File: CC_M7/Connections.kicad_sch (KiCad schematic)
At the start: 11 parts, among them J1 Conn_01x04_Pin, J10 Conn_01x04_Pin, J11 USB_B_Micro, J12 Conn_01x04_Pin, J3 Conn_01x03_Pin, J4 Conn_01x03_Pin, J5 Conn_01x03_Pin, J6 Conn_01x03_Pin, J7 Conn_01x03_Pin, J8 Conn_01x03_Pin

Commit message: 1x04 connectors chosen and added
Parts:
- J1, J10, J12: footprint Connector_PinHeader_1.27mm:PinHeader_1x04_P1.27mm_Vertical -> Connector_Hirose:Hirose_DF13-04P-1.25DSA_1x04_P1.25mm_Vertical
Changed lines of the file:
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@@
 			)
 		)
-		(property "Footprint" "Connector_PinHeader_1.27mm:PinHeader_1x04_P1.27mm_Vertical"
+		(property "Footprint" "Connector_Hirose:Hirose_DF13-04P-1.25DSA_1x04_P1.25mm_Vertical"
 			(at 142.24 157.48 0)
 			(effects
@@
 			)
 		)
-		(property "Footprint" "Connector_PinHeader_1.27mm:PinHeader_1x04_P1.27mm_Vertical"
+		(property "Footprint" "Connector_Hirose:Hirose_DF13-04P-1.25DSA_1x04_P1.25mm_Vertical"
 			(at 52.07 156.21 0)
 			(effects
@@
 			)
 		)
-		(property "Footprint" "Connector_PinHeader_1.27mm:PinHeader_1x04_P1.27mm_Vertical"
+		(property "Footprint" "Connector_Hirose:Hirose_DF13-04P-1.25DSA_1x04_P1.25mm_Vertical"
 			(at 140.97 113.03 0)
 			(effects

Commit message: PCB track draw.
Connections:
- net +BATT renamed VIN_5V
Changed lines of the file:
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@@
 	(wire
 		(pts
-			(xy 147.32 154.94) (xy 154.94 154.94)
+			(xy 147.32 154.94) (xy 149.86 154.94)
 		)
 		(stroke
@@
 	(wire
 		(pts
-			(xy 154.94 152.4) (xy 154.94 154.94)
-		)
-		(stroke
-			(width 0)
-			(type default)
-		)
-	)
-	(wire
-		(pts
 			(xy 128.27 50.8) (xy 133.35 50.8)
 		)
@@
 		)
 	)
+	(global_label "VIN_5V"
+		(shape input)
+		(at 149.86 154.94 0)
+		(fields_autoplaced yes)
+		(effects
+			(font
+				(size 1.27 1.27)
+			)
+			(justify left)
+		)
+		(property "Intersheetrefs" "${INTERSHEET_REFS}"
+			(at 159.1348 154.94 0)
+			(effects
+				(font
+					(size 1.27 1.27)
+				)
+				(justify left)
+				(hide yes)
+			)
+		)
+	)
 	(global_label "J2_36"
 		(shape input)
@@
 					(unit 1)
 				)
-			)
-		)
-	)
-	(symbol
-		(lib_id "power:+BATT")
-		(at 154.94 152.4 0)
-		(unit 1)
-		(exclude_from_sim no)
-		(in_bom yes)
-		(on_board yes)
-		(dnp no)
-		(fields_autoplaced yes)
-		(property "Reference" "#PWR0106"
-			(at 154.94 156.21 0)
-			(effects
-				(font
-					(size 1.27 1.27)
-				)
-				(hide yes)
-			)
-		)
-		(property "Value" "+BATT"
-			(at 154.94 147.32 0)
-			(effects
-				(font
-					(size 1.27 1.27)
-				)
-			)
-		)
-		(property "Footprint" ""
-			(at 154.94 152.4 0)
-			(effects
-				(font
-					(size 1.27 1.27)
-				)
-				(hide yes)
-			)
-		)
-		(property "Datasheet" ""
-			(at 154.94 152.4 0)
-			(effects
-				(font
-					(size 1.27 1.27)
-				)
-				(hide yes)
-			)
-		)
-		(property "Description" "Power symbol creates a global label with name \"+BATT\""
-			(at 154.94 152.4 0)
-			(effects
-				(font
-					(size 1.27 1.27)
-				)
-				(hide yes)
-			)
-		)
-		(pin "1"
-		)
-		(instances
-			(project ""
-				(path "/20c3bbae-00c6-470e-8b69-dc0f665257a3/8b74e690-9be2-433b-8a0a-5eb3a275b61f"
-					(reference "#PWR0106")
-					(unit 1)
-				)

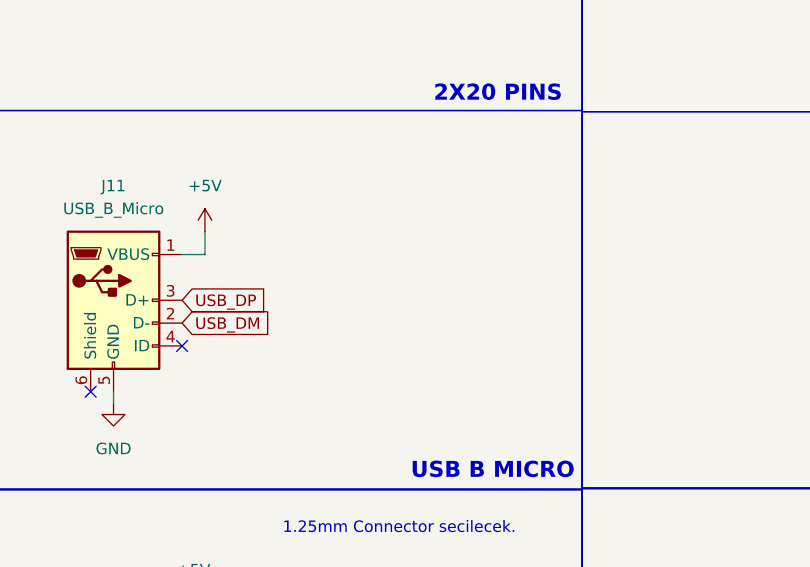
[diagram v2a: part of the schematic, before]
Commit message: USB Pullup added, oscillator capacitors updated.
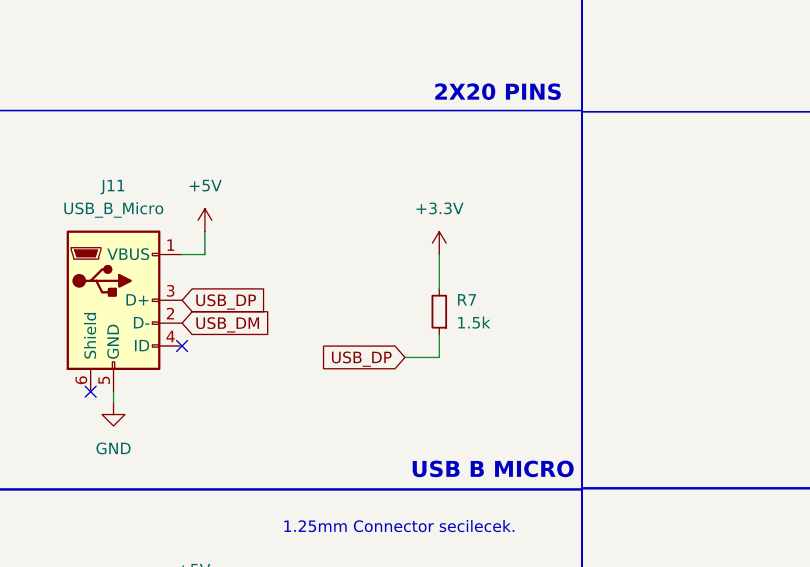
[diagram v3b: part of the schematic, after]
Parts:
- added R7: 1.5k, Resistor_SMD:R_0603_1608Metric, symbol Device:R_Small
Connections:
- net +3.3V: now also R7.2
- net USB_DP: now also R7.1
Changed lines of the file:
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@@
 	(wire
 		(pts
+			(xy 90.805 120.65) (xy 86.995 120.65)
+		)
+		(stroke
+			(width 0)
+			(type default)
+		)
+	)
+	(wire
+		(pts
 			(xy 59.69 156.21) (xy 57.15 156.21)
 		)
@@
 	(wire
 		(pts
+			(xy 90.805 118.11) (xy 90.805 120.65)
+		)
+		(stroke
+			(width 0)
+			(type default)
+		)
+	)
+	(wire
+		(pts
 			(xy 168.91 29.21) (xy 172.72 29.21)
 		)
@@
 	(wire
 		(pts
+			(xy 90.805 109.22) (xy 90.805 113.03)
+		)
+		(stroke
+			(width 0)
+			(type default)
+		)
+	)
+	(wire
+		(pts
 			(xy 50.8 49.53) (xy 35.56 49.53)
 		)
@@
 		)
 	)
+	(global_label "UART4_TX"
+		(shape input)
+		(at 63.5 49.53 0)
+		(fields_autoplaced yes)
+		(effects
+			(font
+				(size 1.27 1.27)
+			)
+			(justify left)
+		)
+		(property "Intersheetrefs" "${INTERSHEET_REFS}"
+			(at 75.4961 49.53 0)
+			(effects
+				(font
+					(size 1.27 1.27)
+				)
+				(justify left)
+				(hide yes)
+			)
+		)
+	)
 	(global_label "CAN2_RX"
 		(shape input)
@@
 		)
 	)
-	(global_label "UART4_TX"
+	(global_label "PA0"
 		(shape input)
-		(at 63.5 49.53 0)
+		(at 63.5 41.91 0)
 		(fields_autoplaced yes)
 		(effects
@@
 		)
 		(property "Intersheetrefs" "${INTERSHEET_REFS}"
-			(at 75.4961 49.53 0)
+			(at 70.0533 41.91 0)
 			(effects
 				(font
@@
 		)
 	)
-	(global_label "PA0"
+	(global_label "UART1_TX"
 		(shape input)
-		(at 63.5 41.91 0)
+		(at 148.59 113.03 0)
 		(fields_autoplaced yes)
 		(effects
@@
 		)
 		(property "Intersheetrefs" "${INTERSHEET_REFS}"
-			(at 70.0533 41.91 0)
+			(at 160.5861 113.03 0)
 			(effects
 				(font
@@
 		)
 	)
-	(global_label "UART1_TX"
+	(global_label "PC15"
 		(shape input)
-		(at 148.59 113.03 0)
+		(at 63.5 54.61 0)
 		(fields_autoplaced yes)
 		(effects
@@
 		)
 		(property "Intersheetrefs" "${INTERSHEET_REFS}"
-			(at 160.5861 113.03 0)
+			(at 71.4442 54.61 0)
 			(effects
 				(font
@@
 		)
 	)
-	(global_label "PC15"
+	(global_label "PC13"
 		(shape input)
-		(at 63.5 54.61 0)
+		(at 63.5 59.69 0)
 		(fields_autoplaced yes)
 		(effects
@@
 		)
 		(property "Intersheetrefs" "${INTERSHEET_REFS}"
-			(at 71.4442 54.61 0)
+			(at 71.4442 59.69 0)
 			(effects
 				(font
@@
 		)
 	)
-	(global_label "PC13"
+	(global_label "USB_DP"
 		(shape input)
-		(at 63.5 59.69 0)
+		(at 86.995 120.65 180)
 		(fields_autoplaced yes)
 		(effects
@@
 				(size 1.27 1.27)
 			)
-			(justify left)
+			(justify right)
 		)
 		(property "Intersheetrefs" "${INTERSHEET_REFS}"
-			(at 71.4442 59.69 0)
+			(at 76.6922 120.65 0)
 			(effects
 				(font
 					(size 1.27 1.27)
 				)
-				(justify left)
+				(justify right)
 				(hide yes)
 			)
@@
 		)
 	)
-	(global_label "J2_38"
+	(global_label "UART4_RX"
 		(shape input)
-		(at 63.5 74.93 0)
+		(at 63.5 46.99 0)
 		(fields_autoplaced yes)
 		(effects
@@
 		)
 		(property "Intersheetrefs" "${INTERSHEET_REFS}"
-			(at 72.0489 74.93 0)
+			(at 75.7985 46.99 0)
 			(effects
 				(font
@@
 		)
 	)
-	(global_label "UART4_RX"
+	(global_label "J2_38"
 		(shape input)
-		(at 63.5 46.99 0)
+		(at 63.5 74.93 0)
 		(fields_autoplaced yes)
 		(effects
@@
 		)
 		(property "Intersheetrefs" "${INTERSHEET_REFS}"
-			(at 75.7985 46.99 0)
+			(at 72.0489 74.93 0)
 			(effects
 				(font
@@
 	)
 	(symbol
+		(lib_id "Device:R_Small")
+		(at 90.805 115.57 180)
+		(unit 1)
+		(exclude_from_sim no)
+		(in_bom yes)
+		(on_board yes)
+		(dnp no)
+		(fields_autoplaced yes)
+		(property "Reference" "R7"
+			(at 92.71 114.2999 0)
+			(effects
+				(font
+					(size 1.27 1.27)
+				)
+				(justify right)
+			)
+		)
+		(property "Value" "1.5k"
+			(at 92.71 116.8399 0)
+			(effects
+				(font
+					(size 1.27 1.27)
+				)
+				(justify right)
+			)
+		)
+		(property "Footprint" "Resistor_SMD:R_0603_1608Metric"
+			(at 90.805 115.57 0)
+			(effects
+				(font
+					(size 1.27 1.27)
+				)
+				(hide yes)
+			)
+		)
+		(property "Datasheet" "~"
+			(at 90.805 115.57 0)
+			(effects
+				(font
+					(size 1.27 1.27)
+				)
+				(hide yes)
+			)
+		)
+		(property "Description" "Resistor, small symbol"
+			(at 90.805 115.57 0)
+			(effects
+				(font
+					(size 1.27 1.27)
+				)
+				(hide yes)
+			)
+		)
+		(pin "1"
+		)
+		(pin "2"
+		)
+		(instances
+			(project "CC_M7"
+				(path "/20c3bbae-00c6-470e-8b69-dc0f665257a3/8b74e690-9be2-433b-8a0a-5eb3a275b61f"
+					(reference "R7")
+					(unit 1)
+				)
+			)
+		)
+	)
+	(symbol
 		(lib_id "power:GND")
 		(at 172.72 34.29 0)
@@
 					(unit 1)
 				)
+			)
+		)
+	)
+	(symbol
+		(lib_id "power:+3.3V")
+		(at 90.805 109.22 0)
+		(unit 1)
+		(exclude_from_sim no)
+		(in_bom yes)
+		(on_board yes)
+		(dnp no)
+		(fields_autoplaced yes)
+		(property "Reference" "#PWR0106"
+			(at 90.805 113.03 0)
+			(effects
+				(font
+					(size 1.27 1.27)
+				)
+				(hide yes)
+			)
+		)
+		(property "Value" "+3.3V"
+			(at 90.805 104.14 0)
+			(effects
+				(font
+					(size 1.27 1.27)
+				)
+			)
+		)
+		(property "Footprint" ""
+			(at 90.805 109.22 0)
+			(effects
+				(font
+					(size 1.27 1.27)
+				)
+				(hide yes)
+			)
+		)
+		(property "Datasheet" ""
+			(at 90.805 109.22 0)
+			(effects
+				(font
+					(size 1.27 1.27)
+				)
+				(hide yes)
+			)
+		)
+		(property "Description" "Power symbol creates a global label with name \"+3.3V\""
+			(at 90.805 109.22 0)
+			(effects
+				(font
+					(size 1.27 1.27)
+				)
+				(hide yes)
+			)
+		)
+		(pin "1"
+		)
+		(instances
+			(project "CC_M7"
+				(path "/20c3bbae-00c6-470e-8b69-dc0f665257a3/8b74e690-9be2-433b-8a0a-5eb3a275b61f"
+					(reference "#PWR0106")
+					(unit 1)
+				)

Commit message: warning check
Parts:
- J3, J4, J5, J6, J7, J8: footprint Connector_PinHeader_2.54mm:PinHeader_1x03_P2.54mm_Vertical -> MountingHole:1x03_2.54vertical
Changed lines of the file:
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@@
 			)
 		)
-		(property "Footprint" "Connector_PinHeader_2.54mm:PinHeader_1x03_P2.54mm_Vertical"
+		(property "Footprint" "MountingHole:1x03_2.54vertical"
 			(at 123.19 71.12 0)
 			(effects
@@
 			)
 		)
-		(property "Footprint" "Connector_PinHeader_2.54mm:PinHeader_1x03_P2.54mm_Vertical"
+		(property "Footprint" "MountingHole:1x03_2.54vertical"
 			(at 163.83 29.21 0)
 			(effects
@@
 			)
 		)
-		(property "Footprint" "Connector_PinHeader_2.54mm:PinHeader_1x03_P2.54mm_Vertical"
+		(property "Footprint" "MountingHole:1x03_2.54vertical"
 			(at 123.19 50.8 0)
 			(effects
@@
 			)
 		)
-		(property "Footprint" "Connector_PinHeader_2.54mm:PinHeader_1x03_P2.54mm_Vertical"
+		(property "Footprint" "MountingHole:1x03_2.54vertical"
 			(at 163.83 71.12 0)
 			(effects
@@
 			)
 		)
-		(property "Footprint" "Connector_PinHeader_2.54mm:PinHeader_1x03_P2.54mm_Vertical"
+		(property "Footprint" "MountingHole:1x03_2.54vertical"
 			(at 123.19 29.21 0)
 			(effects
@@
 			)
 		)
-		(property "Footprint" "Connector_PinHeader_2.54mm:PinHeader_1x03_P2.54mm_Vertical"
+		(property "Footprint" "MountingHole:1x03_2.54vertical"
 			(at 163.83 50.8 0)
 			(effects
